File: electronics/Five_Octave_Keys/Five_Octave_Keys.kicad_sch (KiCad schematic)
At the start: 122 parts, among them SW1 Key Esc, SW10 Key 9, SW11 Key 0, SW12 Key -, SW13 Key =, SW14 Key \, SW15 Key `, SW16 Key Tab, SW17 Key Q, SW18 Key W, SW19 Key E, SW2 Key 1, SW20 Key R, SW21 Key T, SW22 Key Y, SW23 Key U, SW24 Key I, SW25 Key O, SW26 Key P, SW27 Key [, SW28 Key ], SW29 Key BS, SW3 Key 2, SW30 Key Caps, SW31 Key A, SW32 Key S, SW33 Key D, SW34 Key F, SW35 Key G, SW36 Key H, SW37 Key J, SW38 Key K, SW39 Key L, SW4 Key 3, SW40 Key ;, SW41 Key ', SW42 Key Return, SW43 Key Shift, SW44 Key Z, SW45 Key X, SW46 Key C, SW47 Key V, SW48 Key B, SW49 Key N, SW5 Key 4, SW50 Key M, SW51 Key ,, SW52 Key ., SW53 Key /, SW54 Key Shift, SW55 Key Fn, SW56 Key Ctrl, SW57 Key Opt, SW58 Key Cmd, SW59 Key Space, SW6 Key 5, SW60 Key Cmd, SW61 Key MO(1), SW7 Key 6, SW8 Key 7, SW9 Key 8

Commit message: Assign C2128 to the LCSC value of 1N4148WS
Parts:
- D1, D10, D11, D12, D13, D14, D15, D16, D17, D18, D19, D2, D20, D21, D22, D23, D24, D25, D26, D27, D28, D29, D3, D30, D31, D32, D33, D34, D35, D36, D37, D38, D39, D4, D40, D41, D42, D43, D44, D45, D46, D47, D48, D49, D5, D50, D51, D52, D53, D54, D55, D56, D57, D58, D59, D6, D60, D61, D7, D8, D9: LCSC (none) -> C2128
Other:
- title: (none) -> Five Octave - Keys

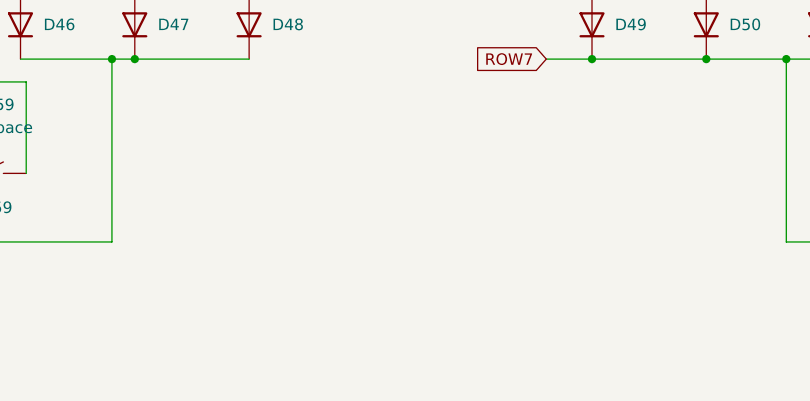
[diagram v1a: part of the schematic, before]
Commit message: Add FFC connector
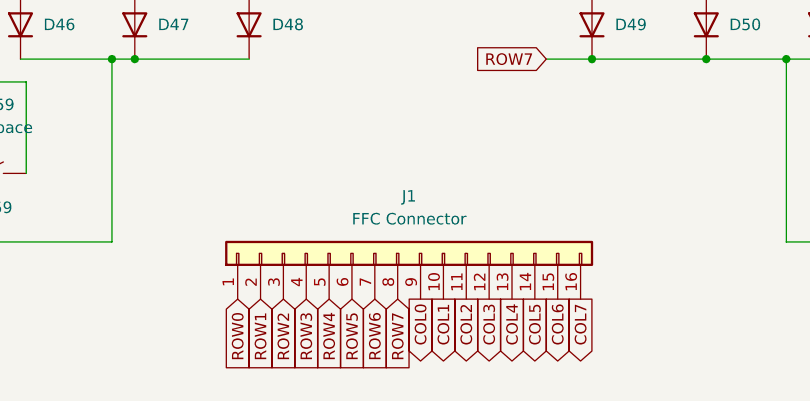
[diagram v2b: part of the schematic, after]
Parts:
- added J1: FFC Connector, Project_Library:JUSHUO_AFC01-S16FCC-00, symbol Connector_Generic:Conn_01x16
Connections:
- net COL0: now also J1.9 (Pin_9)
- net COL1: now also J1.10 (Pin_10)
- net COL2: now also J1.11 (Pin_11)
- net COL3: now also J1.12 (Pin_12)
- net COL4: now also J1.13 (Pin_13)
- net COL5: now also J1.14 (Pin_14)
- net COL6: now also J1.15 (Pin_15)
- net COL7: now also J1.16 (Pin_16)
- net ROW0: now also J1.1 (Pin_1)
- net ROW1: now also J1.2 (Pin_2)
- net ROW2: now also J1.3 (Pin_3)
- net ROW3: now also J1.4 (Pin_4)
- net ROW4: now also J1.5 (Pin_5)
- net ROW5: now also J1.6 (Pin_6)
- net ROW6: now also J1.7 (Pin_7)
- net ROW7: now also J1.8 (Pin_8)
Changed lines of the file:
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@@
   (title_block
     (title "Five Octave - Keys")
-    (date "2023-07-29")
-    (rev "0.0.0")
+    (date "2023-07-30")
+    (rev "0.1.0")
     (comment 1 "https://github.com/takayoshiotake/five-octave-61-key-keyboard")
   )
@@
     (stroke (width 0) (type default))
   )
+  (global_label "ROW6" (shape input) (at 129.54 130.81 270) (fields_autoplaced)
+    (effects (font (size 1.27 1.27)) (justify right))
+    (property "Intersheetrefs" "${INTERSHEET_REFS}" (at 129.54 139.0566 90)
+      (effects (font (size 1.27 1.27)) (justify right) hide)
+    )
+  )
+  (global_label "COL4" (shape output) (at 144.78 130.81 270) (fields_autoplaced)
+    (effects (font (size 1.27 1.27)) (justify right))
+    (property "Intersheetrefs" "${INTERSHEET_REFS}" (at 144.78 138.6333 90)
+      (effects (font (size 1.27 1.27)) (justify right) hide)
+    )
+  )
   (global_label "COL5" (shape output) (at 106.68 25.4 90) (fields_autoplaced)
     (effects (font (size 1.27 1.27)) (justify left))
@@
     )
   )
+  (global_label "ROW0" (shape input) (at 114.3 130.81 270) (fields_autoplaced)
+    (effects (font (size 1.27 1.27)) (justify right))
+    (property "Intersheetrefs" "${INTERSHEET_REFS}" (at 114.3 139.0566 90)
+      (effects (font (size 1.27 1.27)) (justify right) hide)
+    )
+  )
+  (global_label "COL2" (shape output) (at 139.7 130.81 270) (fields_autoplaced)
+    (effects (font (size 1.27 1.27)) (justify right))
+    (property "Intersheetrefs" "${INTERSHEET_REFS}" (at 139.7 138.6333 90)
+      (effects (font (size 1.27 1.27)) (justify right) hide)
+    )
+  )
+  (global_label "COL3" (shape output) (at 142.24 130.81 270) (fields_autoplaced)
+    (effects (font (size 1.27 1.27)) (justify right))
+    (property "Intersheetrefs" "${INTERSHEET_REFS}" (at 142.24 138.6333 90)
+      (effects (font (size 1.27 1.27)) (justify right) hide)
+    )
+  )
+  (global_label "COL6" (shape output) (at 149.86 130.81 270) (fields_autoplaced)
+    (effects (font (size 1.27 1.27)) (justify right))
+    (property "Intersheetrefs" "${INTERSHEET_REFS}" (at 149.86 138.6333 90)
+      (effects (font (size 1.27 1.27)) (justify right) hide)
+    )
+  )
   (global_label "ROW3" (shape input) (at 30.48 104.14 180) (fields_autoplaced)
     (effects (font (size 1.27 1.27)) (justify right))
@@
     )
   )
+  (global_label "ROW4" (shape input) (at 124.46 130.81 270) (fields_autoplaced)
+    (effects (font (size 1.27 1.27)) (justify right))
+    (property "Intersheetrefs" "${INTERSHEET_REFS}" (at 124.46 139.0566 90)
+      (effects (font (size 1.27 1.27)) (justify right) hide)
+    )
+  )
   (global_label "ROW6" (shape input) (at 141.605 83.82 180) (fields_autoplaced)
     (effects (font (size 1.27 1.27)) (justify right))
@@
     )
   )
+  (global_label "ROW5" (shape input) (at 127 130.81 270) (fields_autoplaced)
+    (effects (font (size 1.27 1.27)) (justify right))
+    (property "Intersheetrefs" "${INTERSHEET_REFS}" (at 127 139.0566 90)
+      (effects (font (size 1.27 1.27)) (justify right) hide)
+    )
+  )
+  (global_label "ROW1" (shape input) (at 116.84 130.81 270) (fields_autoplaced)
+    (effects (font (size 1.27 1.27)) (justify right))
+    (property "Intersheetrefs" "${INTERSHEET_REFS}" (at 116.84 139.0566 90)
+      (effects (font (size 1.27 1.27)) (justify right) hide)
+    )
+  )
   (global_label "COL4" (shape output) (at 93.98 25.4 90) (fields_autoplaced)
     (effects (font (size 1.27 1.27)) (justify left))
@@
     )
   )
+  (global_label "ROW7" (shape input) (at 132.08 130.81 270) (fields_autoplaced)
+    (effects (font (size 1.27 1.27)) (justify right))
+    (property "Intersheetrefs" "${INTERSHEET_REFS}" (at 132.08 139.0566 90)
+      (effects (font (size 1.27 1.27)) (justify right) hide)
+    )
+  )
   (global_label "COL3" (shape output) (at 81.28 25.4 90) (fields_autoplaced)
     (effects (font (size 1.27 1.27)) (justify left))
@@
     )
   )
+  (global_label "ROW3" (shape input) (at 121.92 130.81 270) (fields_autoplaced)
+    (effects (font (size 1.27 1.27)) (justify right))
+    (property "Intersheetrefs" "${INTERSHEET_REFS}" (at 121.92 139.0566 90)
+      (effects (font (size 1.27 1.27)) (justify right) hide)
+    )
+  )
+  (global_label "COL1" (shape output) (at 137.16 130.81 270) (fields_autoplaced)
+    (effects (font (size 1.27 1.27)) (justify right))
+    (property "Intersheetrefs" "${INTERSHEET_REFS}" (at 137.16 138.6333 90)
+      (effects (font (size 1.27 1.27)) (justify right) hide)
+    )
+  )
   (global_label "COL0" (shape output) (at 157.48 25.4 90) (fields_autoplaced)
     (effects (font (size 1.27 1.27)) (justify left))
@@
     )
   )
+  (global_label "ROW2" (shape input) (at 119.38 130.81 270) (fields_autoplaced)
+    (effects (font (size 1.27 1.27)) (justify right))
+    (property "Intersheetrefs" "${INTERSHEET_REFS}" (at 119.38 139.0566 90)
+      (effects (font (size 1.27 1.27)) (justify right) hide)
+    )
+  )
   (global_label "COL0" (shape output) (at 43.18 25.4 90) (fields_autoplaced)
     (effects (font (size 1.27 1.27)) (justify left))
@@
     )
   )
+  (global_label "COL5" (shape output) (at 147.32 130.81 270) (fields_autoplaced)
+    (effects (font (size 1.27 1.27)) (justify right))
+    (property "Intersheetrefs" "${INTERSHEET_REFS}" (at 147.32 138.6333 90)
+      (effects (font (size 1.27 1.27)) (justify right) hide)
+    )
+  )
   (global_label "ROW1" (shape input) (at 30.48 63.5 180) (fields_autoplaced)
     (effects (font (size 1.27 1.27)) (justify right))
@@
     )
   )
+  (global_label "COL0" (shape output) (at 134.62 130.81 270) (fields_autoplaced)
+    (effects (font (size 1.27 1.27)) (justify right))
+    (property "Intersheetrefs" "${INTERSHEET_REFS}" (at 134.62 138.6333 90)
+      (effects (font (size 1.27 1.27)) (justify right) hide)
+    )
+  )
   (global_label "COL7" (shape output) (at 246.38 25.4 90) (fields_autoplaced)
     (effects (font (size 1.27 1.27)) (justify left))
@@
     )
   )
+  (global_label "COL7" (shape output) (at 152.4 130.81 270) (fields_autoplaced)
+    (effects (font (size 1.27 1.27)) (justify right))
+    (property "Intersheetrefs" "${INTERSHEET_REFS}" (at 152.4 138.6333 90)
+      (effects (font (size 1.27 1.27)) (justify right) hide)
+    )
+  )
   (global_label "COL6" (shape output) (at 233.68 25.4 90) (fields_autoplaced)
     (effects (font (size 1.27 1.27)) (justify left))
@@
         )
       )
+    )
+  )
+  (symbol (lib_id "Connector_Generic:Conn_01x16") (at 132.08 125.73 90) (unit 1)
+    (in_bom yes) (on_board yes) (dnp no) (fields_autoplaced)
+    (property "Reference" "J1" (at 133.35 119.38 90)
+      (effects (font (size 1.27 1.27)))
+    )
+    (property "Value" "FFC Connector" (at 133.35 121.92 90)
+      (effects (font (size 1.27 1.27)))
+    )
+    (property "Footprint" "Project_Library:JUSHUO_AFC01-S16FCC-00" (at 132.08 125.73 0)
+      (effects (font (size 1.27 1.27)) hide)
+    )
+    (property "Datasheet" "~" (at 132.08 125.73 0)
+      (effects (font (size 1.27 1.27)) hide)
+    )
+    (property "LCSC" "C262272" (at 132.08 125.73 90)
+      (effects (font (size 1.27 1.27)) hide)
+    )
+    (pin "1")
+    (pin "10")
+    (pin "11")
+    (pin "12")
+    (pin "13")
+    (pin "14")
+    (pin "15")
+    (pin "16")
+    (pin "2")
+    (pin "3")
+    (pin "4")
+    (pin "5")
+    (pin "6")
+    (pin "7")
+    (pin "8")
+    (pin "9")
+    (instances
+      (project "Five_Octave_Keys"
+        (path "/0d6ccbdd-8445-429e-a23a-56d9fd96e05e"
+          (reference "J1") (unit 1)
+        )
+      )

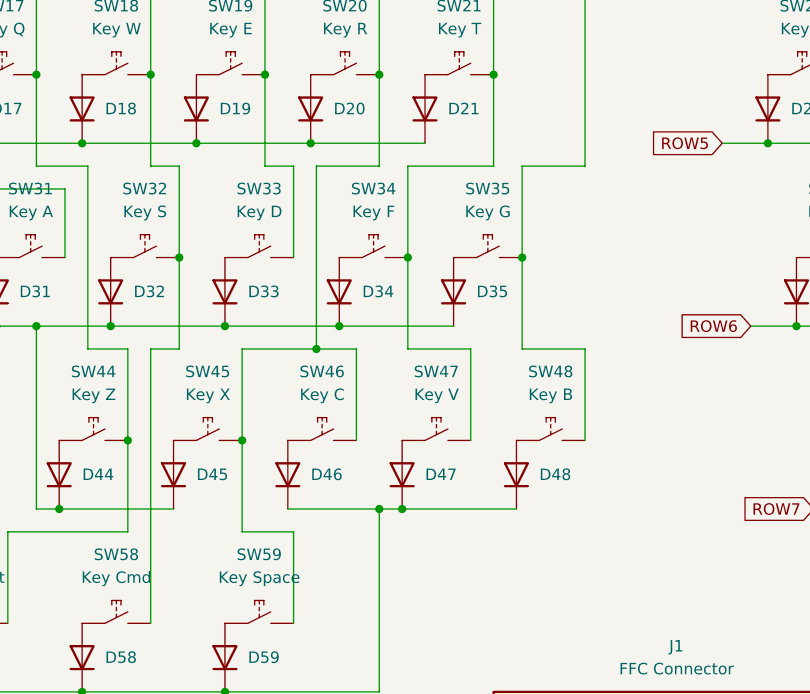
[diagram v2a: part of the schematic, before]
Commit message: Adjust key-matrix
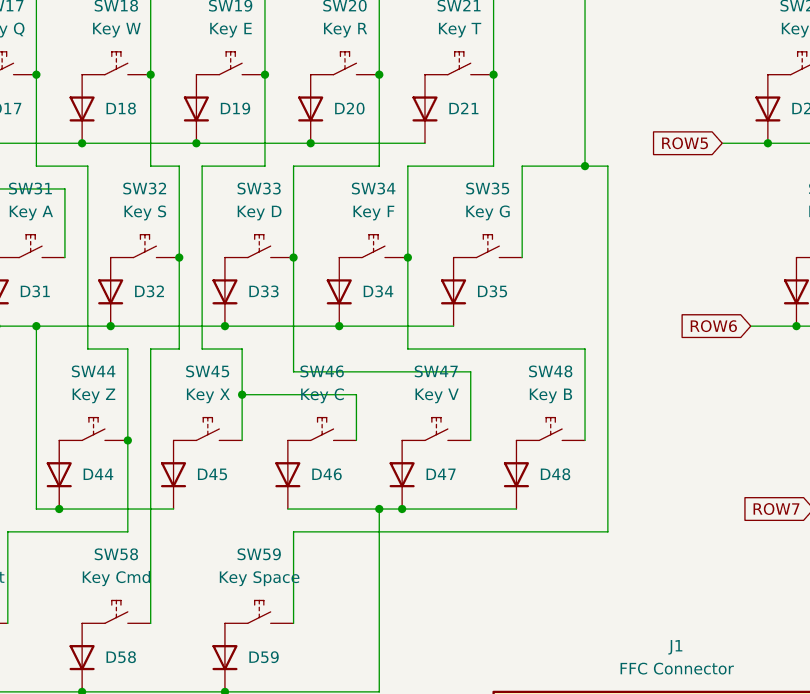
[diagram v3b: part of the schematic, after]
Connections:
- net COL4: now also SW45.2, SW46.2; no longer SW33.2
- net COL5: now also SW33.2, SW47.2; no longer SW45.2, SW46.2, SW59.2
- net COL6: now also SW48.2; no longer SW47.2
- net COL7: now also SW59.2; no longer SW48.2
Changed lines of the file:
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@@
   (title_block
     (title "Five Octave - Keys")
-    (date "2023-07-30")
-    (rev "0.1.0")
+    (date "2023-08-02")
+    (rev "0.2.0")
     (comment 1 "https://github.com/takayoshiotake/five-octave-61-key-keyboard")
   )
@@
   (junction (at 70.485 83.82) (diameter 0) (color 0 0 0 0)
   )
-  (junction (at 93.345 86.36) (diameter 0) (color 0 0 0 0)
-  )
   (junction (at 181.61 63.5) (diameter 0) (color 0 0 0 0)
   )
@@
   (junction (at 143.51 63.5) (diameter 0) (color 0 0 0 0)
   )
-  (junction (at 116.205 76.2) (diameter 0) (color 0 0 0 0)
-  )
   (junction (at 179.705 76.2) (diameter 0) (color 0 0 0 0)
   )
@@
   (junction (at 43.18 76.2) (diameter 0) (color 0 0 0 0)
   )
+  (junction (at 85.09 91.44) (diameter 0) (color 0 0 0 0)
+  )
   (junction (at 83.185 124.46) (diameter 0) (color 0 0 0 0)
   )
@@
   (junction (at 194.31 63.5) (diameter 0) (color 0 0 0 0)
   )
-  (junction (at 85.09 96.52) (diameter 0) (color 0 0 0 0)
-  )
   (junction (at 246.38 35.56) (diameter 0) (color 0 0 0 0)
   )
@@
   (junction (at 51.435 124.46) (diameter 0) (color 0 0 0 0)
   )
+  (junction (at 90.805 76.2) (diameter 0) (color 0 0 0 0)
+  )
   (junction (at 184.785 83.82) (diameter 0) (color 0 0 0 0)
   )
@@
   (junction (at 100.33 55.88) (diameter 0) (color 0 0 0 0)
   )
+  (junction (at 123.19 66.04) (diameter 0) (color 0 0 0 0)
+  )
   (wire (pts (xy 162.56 43.18) (xy 175.26 43.18))
     (stroke (width 0) (type default))
   )
+  (wire (pts (xy 90.805 76.2) (xy 90.805 88.9))
+    (stroke (width 0) (type default))
+  )
+  (wire (pts (xy 125.73 66.04) (xy 123.19 66.04))
+    (stroke (width 0) (type default))
+  )
   (wire (pts (xy 151.13 66.04) (xy 151.13 55.88))
     (stroke (width 0) (type default))
@@
     (stroke (width 0) (type default))
   )
+  (wire (pts (xy 80.645 66.04) (xy 80.645 86.36))
+    (stroke (width 0) (type default))
+  )
   (wire (pts (xy 35.56 63.5) (xy 54.61 63.5))
     (stroke (width 0) (type default))
@@
     (stroke (width 0) (type default))
   )
-  (wire (pts (xy 85.09 96.52) (xy 85.09 106.68))
-    (stroke (width 0) (type default))
-  )
   (wire (pts (xy 179.705 86.36) (xy 179.705 76.2))
     (stroke (width 0) (type default))
@@
     (stroke (width 0) (type default))
   )
+  (wire (pts (xy 103.505 86.36) (xy 123.19 86.36))
+    (stroke (width 0) (type default))
+  )
   (wire (pts (xy 214.63 66.04) (xy 214.63 55.88))
     (stroke (width 0) (type default))
@@
     (stroke (width 0) (type default))
   )
+  (wire (pts (xy 123.19 86.36) (xy 123.19 96.52))
+    (stroke (width 0) (type default))
+  )
   (wire (pts (xy 119.38 25.4) (xy 119.38 35.56))
     (stroke (width 0) (type default))
@@
     (stroke (width 0) (type default))
   )
+  (wire (pts (xy 97.79 91.44) (xy 97.79 96.52))
+    (stroke (width 0) (type default))
+  )
   (wire (pts (xy 143.51 63.5) (xy 156.21 63.5))
     (stroke (width 0) (type default))
@@
     (stroke (width 0) (type default))
   )
-  (wire (pts (xy 103.505 86.36) (xy 110.49 86.36))
-    (stroke (width 0) (type default))
-  )
   (wire (pts (xy 227.33 55.88) (xy 227.33 45.72))
     (stroke (width 0) (type default))
@@
     (stroke (width 0) (type default))
   )
+  (wire (pts (xy 80.645 86.36) (xy 85.09 86.36))
+    (stroke (width 0) (type default))
+  )
   (wire (pts (xy 83.185 124.46) (xy 100.33 124.46))
     (stroke (width 0) (type default))
@@
     (stroke (width 0) (type default))
   )
+  (wire (pts (xy 85.09 91.44) (xy 97.79 91.44))
+    (stroke (width 0) (type default))
+  )
+  (wire (pts (xy 110.49 88.9) (xy 110.49 96.52))
+    (stroke (width 0) (type default))
+  )
   (wire (pts (xy 154.305 86.36) (xy 154.305 76.2))
     (stroke (width 0) (type default))
@@
     (stroke (width 0) (type default))
   )
-  (wire (pts (xy 123.19 86.36) (xy 123.19 96.52))
-    (stroke (width 0) (type default))
-  )
   (wire (pts (xy 163.83 45.72) (xy 170.18 45.72))
     (stroke (width 0) (type default))
@@
     (stroke (width 0) (type default))
   )
-  (wire (pts (xy 85.09 106.68) (xy 90.805 106.68))
-    (stroke (width 0) (type default))
-  )
   (wire (pts (xy 151.13 45.72) (xy 157.48 45.72))
     (stroke (width 0) (type default))
@@
     (stroke (width 0) (type default))
   )
-  (wire (pts (xy 116.205 86.36) (xy 123.19 86.36))
-    (stroke (width 0) (type default))
-  )
   (wire (pts (xy 214.63 45.72) (xy 220.98 45.72))
     (stroke (width 0) (type default))
@@
     (stroke (width 0) (type default))
   )
-  (wire (pts (xy 85.09 96.52) (xy 85.09 86.36))
+  (wire (pts (xy 85.09 86.36) (xy 85.09 91.44))
     (stroke (width 0) (type default))
   )
@@
     (stroke (width 0) (type default))
   )
-  (wire (pts (xy 93.345 86.36) (xy 97.79 86.36))
-    (stroke (width 0) (type default))
-  )
   (wire (pts (xy 214.63 55.88) (xy 214.63 45.72))
     (stroke (width 0) (type default))
@@
     (stroke (width 0) (type default))
   )
+  (wire (pts (xy 90.805 88.9) (xy 110.49 88.9))
+    (stroke (width 0) (type default))
+  )
   (wire (pts (xy 186.69 86.36) (xy 179.705 86.36))
     (stroke (width 0) (type default))
@@
     (stroke (width 0) (type default))
   )
+  (wire (pts (xy 90.805 106.68) (xy 125.73 106.68))
+    (stroke (width 0) (type default))
+  )
   (wire (pts (xy 189.23 66.04) (xy 189.23 55.88))
     (stroke (width 0) (type default))
@@
     (stroke (width 0) (type default))
   )
+  (wire (pts (xy 87.63 66.04) (xy 80.645 66.04))
+    (stroke (width 0) (type default))
+  )
   (wire (pts (xy 113.03 66.04) (xy 103.505 66.04))
     (stroke (width 0) (type default))
@@
     (stroke (width 0) (type default))
   )
-  (wire (pts (xy 93.345 66.04) (xy 93.345 86.36))
+  (wire (pts (xy 90.805 66.04) (xy 90.805 76.2))
     (stroke (width 0) (type default))
   )
@@
     (stroke (width 0) (type default))
   )
-  (wire (pts (xy 90.805 76.2) (xy 90.805 66.04))
-    (stroke (width 0) (type default))
-  )
   (wire (pts (xy 175.26 104.14) (xy 179.07 104.14))
     (stroke (width 0) (type default))
@@
     (stroke (width 0) (type default))
   )
-  (wire (pts (xy 90.805 66.04) (xy 87.63 66.04))
-    (stroke (width 0) (type default))
-  )
   (wire (pts (xy 30.48 43.18) (xy 35.56 43.18))
     (stroke (width 0) (type default))
   )
-  (wire (pts (xy 85.09 86.36) (xy 93.345 86.36))
-    (stroke (width 0) (type default))
-  )
   (wire (pts (xy 62.23 55.88) (xy 62.23 45.72))
     (stroke (width 0) (type default))
@@
     (stroke (width 0) (type default))
   )
+  (wire (pts (xy 125.73 66.04) (xy 125.73 106.68))
+    (stroke (width 0) (type default))
+  )
   (wire (pts (xy 172.085 83.82) (xy 184.785 83.82))
     (stroke (width 0) (type default))
@@
     (stroke (width 0) (type default))
   )
-  (wire (pts (xy 97.79 96.52) (xy 97.79 86.36))
-    (stroke (width 0) (type default))
-  )
   (wire (pts (xy 74.93 116.84) (xy 74.93 86.36))
     (stroke (width 0) (type default))
@@
     (stroke (width 0) (type default))
   )
-  (wire (pts (xy 100.33 66.04) (xy 93.345 66.04))
-    (stroke (width 0) (type default))
-  )
-  (wire (pts (xy 116.205 76.2) (xy 116.205 86.36))
+  (wire (pts (xy 90.805 66.04) (xy 100.33 66.04))
     (stroke (width 0) (type default))
   )
@@
     (stroke (width 0) (type default))
   )
+  (wire (pts (xy 85.09 91.44) (xy 85.09 96.52))
+    (stroke (width 0) (type default))
+  )
   (wire (pts (xy 149.86 43.18) (xy 162.56 43.18))
     (stroke (width 0) (type default))
   )
-  (wire (pts (xy 110.49 96.52) (xy 110.49 86.36))
-    (stroke (width 0) (type default))
-  )
